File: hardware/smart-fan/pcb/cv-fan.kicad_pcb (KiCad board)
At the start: 2 copper layers, 88.7 x 94.8 mm, 41 parts, among them J1 2P 5.08mm, J2 2P 5.08mm, J3 3P 5.08mm, K1 SRD-05VDC-SL-C, Q1 S8050, SW1 Tactile 6mm, U1 ESP32-WROOM-32E (4MB), U2 AMS1117-3.3, U3 MCP6002

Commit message: hardware: fix mains isolation barrier gaps, add load-controller PCB
Adds the 13th board (ultra-compact dual-channel load controller: ESP32-C3,
opto+relay channel, MOSFET PWM channel, USB-C, AP2112K LDO, USBLC6 ESD) and
regenerates all 12 existing boards, which were stale with respect to earlier
relay-pinout and LED-polarity fixes.

The substantive change is to the mains isolation barrier. It is a keepout band
the router must not cross, deliberately cut where a component straddles it
because there the isolation is provided by the part's package. Three linked
defects made those cuts unsafe, each only visible once the previous was fixed:

1. The cut removed the barrier across the full band width for the straddling
   part's whole height, while the ISO_BRIDGE area that excuses the gap covered
   only the part itself. The router used the leftover strip beside the part to
   bring +5V within 6.99 mm of AC_N against an 8.0 mm reinforced creepage rule.
2. Straddling parts can overlap in y, so cutting per part put one part's
   keepout on another part's pads. The exempt x-ranges are now unioned per
   strip by a sweep line.
3. The rule only relaxes for items insideArea('ISO_BRIDGE'). With the hole the
   same size as the area, a track could hug the hole's edge without being
   contained in it, so the rule fired anyway and the router had no way to know.
   The hole is now the part's pad bbox + 0.3 mm, strictly inside ISO_BRIDGE at
   the footprint bbox + 0.6 mm.

The tighter hole leaves mains nets less room to reach bridge pads, so some
boards report more unconnected items. That is deliberate: those are documented
hand-routing items, whereas a creepage violation is a safety defect.

Also fixed in the generator:
- _pad_shape() derived a pad's layers from PAD::GetLayer(), which returns F.Cu
  even for pads on B.Cu. Every back-side pad became a phantom obstacle on the
  front, blocking legal paths there while hiding the real one behind. Only
  IsOnLayer() is truthful.
- Castella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
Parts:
- moved JP 47.5 mm to (181.0, 152.8)
- moved LED0 47.5 mm to (160.3, 155.6)
- moved R2 47.5 mm to (172.0, 144.8)
- moved R3 47.5 mm to (153.0, 144.8)
- moved R4 47.5 mm to (157.4, 144.8)
- moved R9 47.5 mm to (159.5, 151.5)
- moved C2 47.5 mm to (153.4, 151.1)
- moved C3 47.5 mm to (157.5, 136.8)
- moved C4 47.5 mm to (162.0, 136.8)
- moved C5 47.5 mm to (166.5, 136.8)
- moved C6 47.5 mm to (171.0, 136.8)
- moved Cf 47.5 mm to (153.0, 136.8)
- moved J2 47.5 mm to (154.3, 141.5)
- moved PC1 47.5 mm to (176.0, 145.9)
- moved Qm 47.5 mm to (166.1, 150.8)
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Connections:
- K1 pad 2: FAN_RELAY_SW -> +5V
- K1 pad 3: +5V -> FAN_RELAY_SW
- K1 pad 4: FAN_RELAY_COIL -> N$K1.4
- K1 pad 5: N$K1.5 -> FAN_RELAY_COIL
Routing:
- net SPEED_PWM_PIN_OUT: track 69.4 -> 0.00 mm, vias 2 -> 0
- net BTN_PIN: track 69.6 -> 25.1 mm
- net AC_N: track 42.2 -> 0.00 mm
- net FAN_RELAY_COIL: track 57.8 -> 86.4 mm
- net FAN_RELAY: track 64.6 -> 36.8 mm, vias 1 -> 3
- net AC_L_FUSED: track 32.1 -> 5.00 mm
- net FAN_RELAY_SW: track 26.7 -> 0.00 mm
- net SPEED_PWM_PIN: track 65.7 -> 42.9 mm, vias 3 -> 1
- net +5V: track 174.2 -> 192.6 mm
- net +3V3: track 145.8 -> 127.9 mm, vias 0 -> 2
- net UART_TX: track 33.8 -> 50.4 mm
- net UART_RX: track 35.8 -> 51.1 mm, vias 1 -> 0
- net SPEED_PWM_PIN_B: track 14.1 -> 9.54 mm
- net FAN_RELAY_OPT: track 10.4 -> 12.6 mm, vias 0 -> 1
- net EN: track 42.8 -> 44.5 mm, vias 3 -> 1
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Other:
- outline, holes or cut-outs redrawn
- board text removed: "!! MAINS !!"

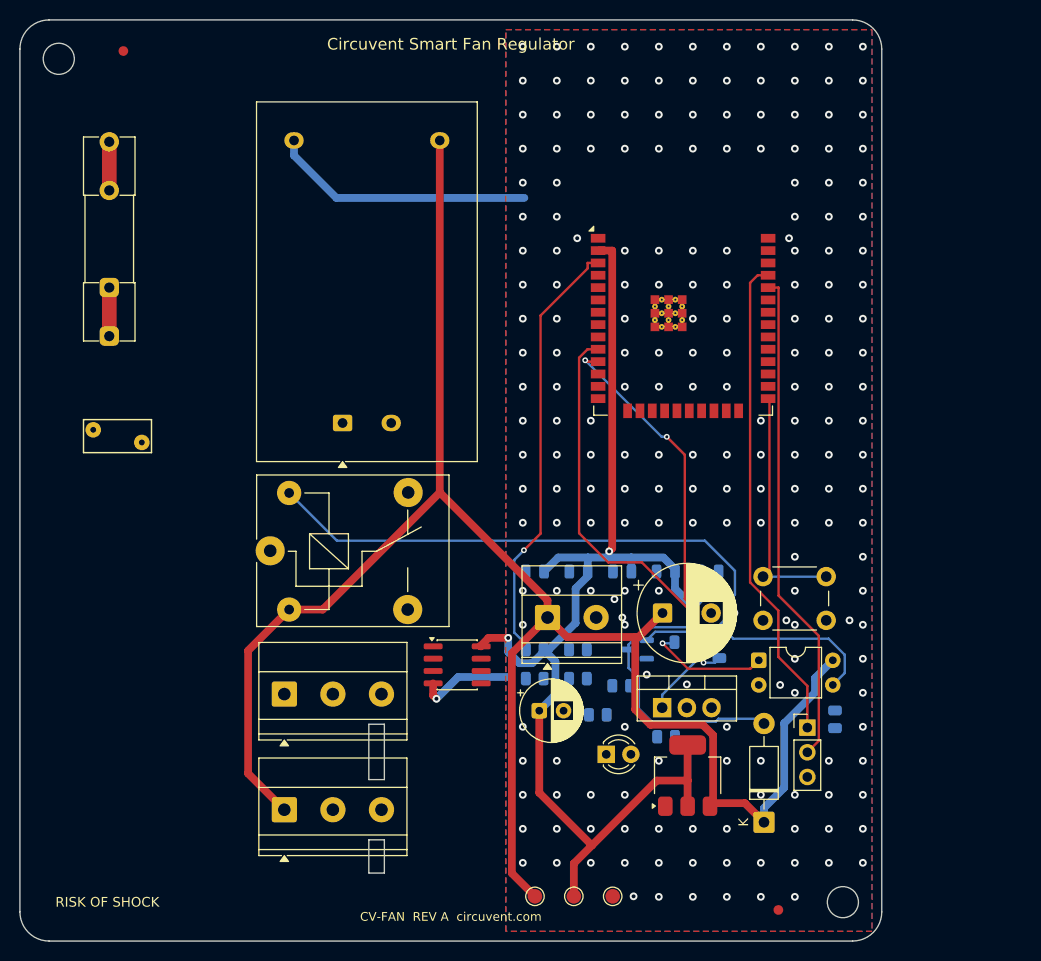
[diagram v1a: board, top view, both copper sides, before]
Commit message: Release 1.10.0, and stop shipping permissions the app never uses
Cut 1.10.0 (versionCode 12) and built it: AAB 38 MB, APK 83 MB, signed with the
upload key, JS bundle embedded.

Checking the generated manifest before writing the Play listing turned up
permissions no one had asked for. Every one of them is printed on the store page
for users to read before they install:

  RECORD_AUDIO          expo-camera asks for the microphone so video can be
                        recorded with sound. This app only ever puts the camera
                        in barcode mode to read a QR label, and expo-speech is
                        output-only - it speaks, it does not listen. Left in,
                        Play lists "Microphone" against a home-control app,
                        which is alarming, unexplainable and untrue.
  SYSTEM_ALERT_WINDOW   React Native's development overlay, useless in a release
                        build and shown to users as "Display over other apps".
  READ/WRITE_EXTERNAL_STORAGE
                        Legacy storage access nothing here touches.

Stripped via android.blockedPermissions. That emits tools:node="remove", which
is a merge instruction rather than a guarantee, so it was checked against the
finished artifact with aapt2 rather than the source manifest - all four are
absent from the APK.

NEARBY_WIFI_DEVICES now carries neverForLocation. Android otherwise treats it as
location-capable, because knowing which networks are in range is enough to place
someone, and Play's data safety review treats it the same way. The app uses it
only to join a new device's setup hotspot. That flag is a promise, so the plugin
says plainly that it has to come off if scan results are ever used positionally.

What is left is defensible: location for Wi-Fi onboarding (Android requires it),
camera for the QR label, nearby-devices flagged as non-positional.

Added mobile/store/listing with the text Play asks for - title, short and full
descriptions, and what'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
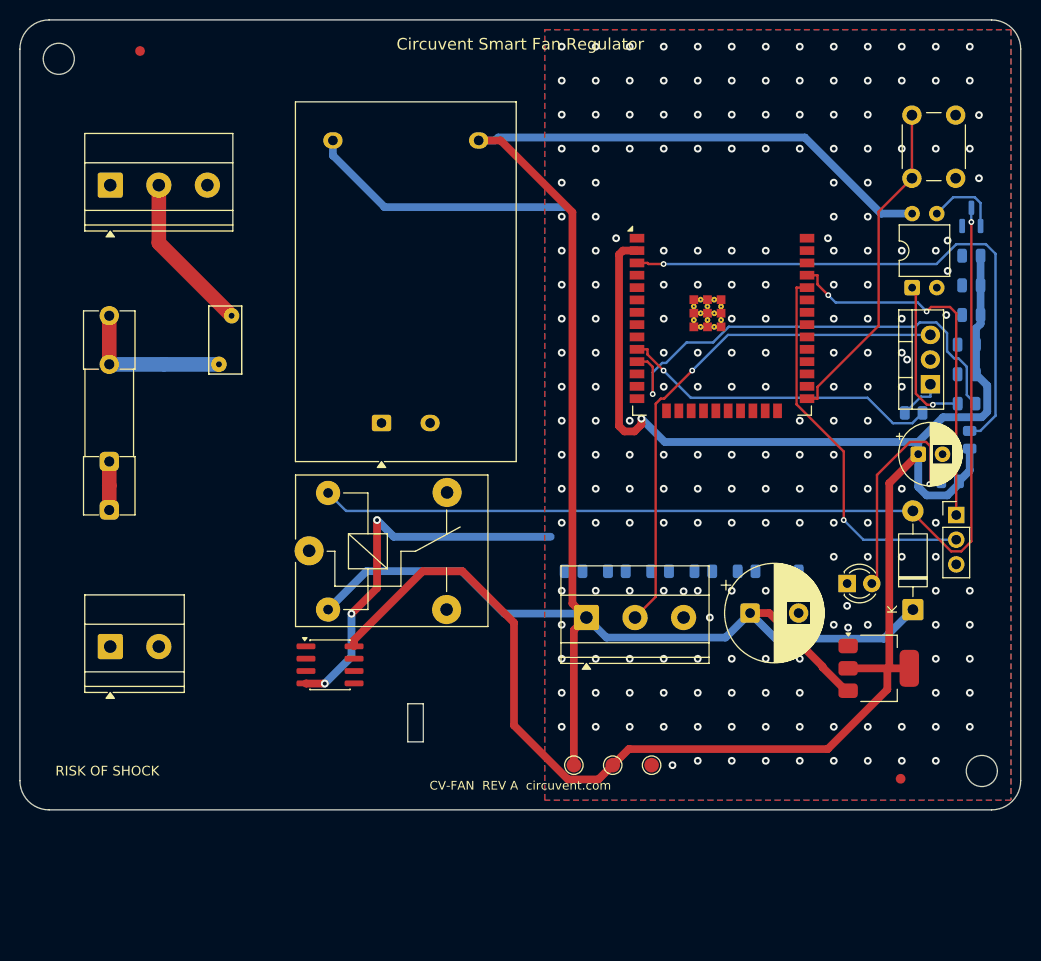
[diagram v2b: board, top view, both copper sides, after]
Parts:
- moved Q1 56.2 mm to (197.9, 100.3), turned to 90 degrees
- moved Cf 55.4 mm to (197.9, 104.3)
- moved J1 55.4 mm to (109.3, 97.0)
- moved C3 50.0 mm to (197.9, 107.3)
- moved R3 49.7 mm to (197.8, 123.2), turned to 90 degrees
- moved C2 47.1 mm to (192.5, 124.7)
- moved J2 45.1 mm to (109.3, 144.5)
- moved C4 44.6 mm to (197.9, 110.4)
- moved SW1 43.8 mm to (191.8, 96.3), turned to 90 degrees
- moved Qm 43.2 mm to (193.7, 117.5), turned to 90 degrees
- moved R4 42.0 mm to (195.7, 127.5)
- moved PC1 41.5 mm to (191.8, 107.6), turned to 90 degrees
- moved C5 38.8 mm to (197.4, 113.4)
- moved R1 38.1 mm to (197.4, 119.5)
- moved J3 36.9 mm to (158.3, 141.5)
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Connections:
- J1 pad 3: SPEED_PWM_PIN_OUT -> PE
- J2 pad 1: +5V -> FAN_RELAY_SW
- J2 pad 2: GND -> AC_N
- J3 pad 2: FAN_RELAY_SW -> SPEED_PWM_PIN_OUT
- J3 pad 3: AC_N -> GND
- LED0 pad 1: N$LED0.1 -> GND
- LED0 pad 2: N$LED0.2 -> LED0_A
- R4 pad 1: N$R4.1 -> +3V3
- R4 pad 2: N$R4.2 -> LED0_A
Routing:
- net +3V3: track 127.9 -> 200.6 mm, vias 2 -> 1
- net SPEED_PWM_PIN_OUT: track 0.00 -> 54.1 mm, vias 0 -> 1
- net GND: track 37.3 -> 67.6 mm, vias 215 -> 216
- net LED0_A: track 0.00 -> 23.8 mm, vias 0 -> 1
- net FAN_RELAY_DRV: track 25.3 -> 7.81 mm
- net FAN_RELAY_COIL: track 86.4 -> 103.6 mm, vias 0 -> 1
- net AC_N: track 0.00 -> 16.5 mm
- net EN: track 44.5 -> 58.2 mm
- net UART_TX: track 50.4 -> 38.7 mm, vias 0 -> 2
- net FAN_RELAY: track 36.8 -> 48.5 mm, vias 3 -> 1
- net UART_RX: track 51.1 -> 39.4 mm, vias 0 -> 1
- net AC_L_FUSED: track 5.00 -> 16.3 mm
- net SPEED_PWM_PIN: track 42.9 -> 33.3 mm
- net BTN_PIN: track 25.1 -> 34.3 mm
- net +5V: track 192.6 -> 200.2 mm
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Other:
- board size 88.7 x 94.8 mm -> 103 x 81.3 mm
